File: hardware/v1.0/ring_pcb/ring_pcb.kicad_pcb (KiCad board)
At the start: 2 copper layers, 17.8 x 17.8 mm, 14 parts

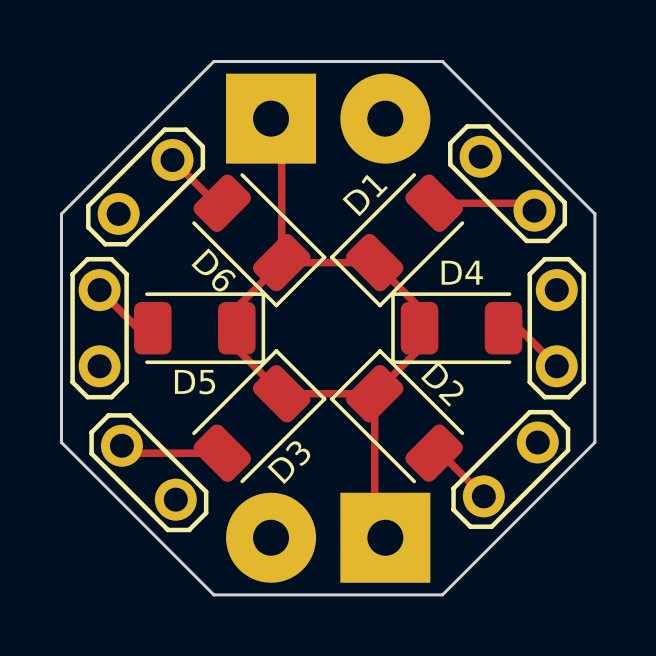
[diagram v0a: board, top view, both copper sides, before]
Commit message: Update pcb to v0.2 for new mounting plan
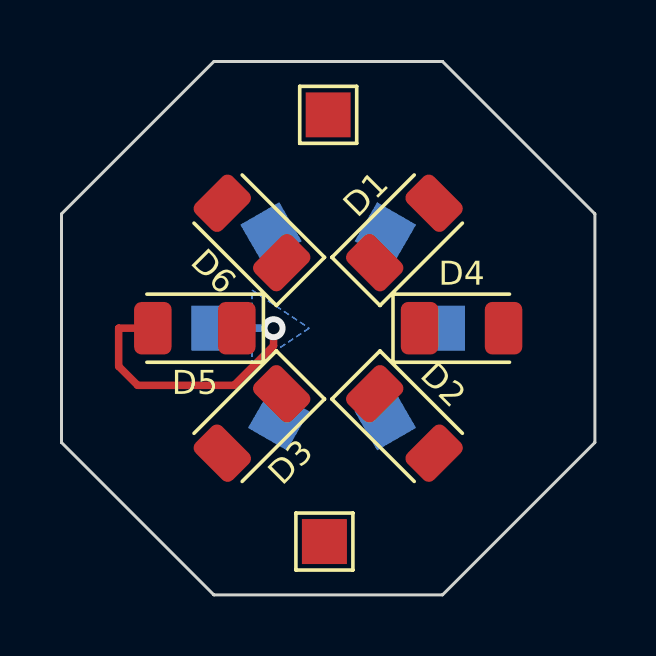
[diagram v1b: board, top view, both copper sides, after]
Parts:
- TP1, TP2, TP3, TP4, TP5, TP6: value TestPoint_2Pole -> TestPoint; footprint TestPoint:TestPoint_2Pads_Pitch2.54mm_Drill0.8mm -> TestPoint:TestPoint_Pad_1.5x1.5mm; moved to B.Cu
- TP7, TP8: value TestPoint_2Pole -> TestPoint; footprint Connector_Wire:SolderWirePad_1x02_P3.81mm_Drill1.2mm -> TestPoint:TestPoint_Pad_1.5x1.5mm
- moved TP2 11.4 mm to (133.3, 99.1), turned to 180 degrees
- moved TP3 11.3 mm to (139.1, 95.9), turned to 60 degrees
- moved TP4 10.2 mm to (135.5, 102.1), turned to 60 degrees
- moved TP5 9.69 mm to (139.1, 102.1), turned to -60 degrees
- moved TP1 5.85 mm to (141.0, 99.1), turned to 180 degrees
- moved TP6 5.12 mm to (135.3, 95.9), turned to -60 degrees
- moved TP8 2.04 mm to (137.0, 106.2), turned to 0 degrees
- moved TP7 1.91 mm to (137.2, 91.9)
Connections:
- D1 pad 1: GND -> Net-(D4-Pad1)
- D2 pad 1: GND -> Net-(D4-Pad1)
- D2 pad 2: Net-(D2-Pad2) -> /N2
- D3 pad 1: GND -> Net-(D4-Pad1)
- D4 pad 1: GND -> Net-(D4-Pad1)
- D5 pad 1: GND -> Net-(D4-Pad1)
- TP1 pad 1: no_connect_8 -> Net-(D4-Pad2)
- TP2 pad 1: no_connect_9 -> Net-(D5-Pad2)
- TP3 pad 1: no_connect_10 -> Net-(D1-Pad2)
- TP4 pad 1: no_connect_11 -> Net-(D3-Pad2)
- TP5 pad 1: no_connect_12 -> /N2
- TP6 pad 1: no_connect_13 -> Net-(D6-Pad2)
- TP7 pad 1: GND -> Net-(D4-Pad1)
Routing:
- net GND: track 27.3 -> 0.00 mm
- net Net-(D5-Pad2): track 2.30 -> 11.0 mm, vias 0 -> 1
- net Net-(D3-Pad2): track 3.45 -> 0.00 mm
- net Net-(D1-Pad2): track 3.45 -> 0.00 mm
- net Net-(D4-Pad2): track 2.30 -> 0.00 mm
- net Net-(D6-Pad2): track 2.26 -> 0.00 mm
- net Net-(D2-Pad2): track 2.26 -> 0.00 mm
- added copper zone on B.Cu, net /N2
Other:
- board text added: "Lantern Ring v0.2 OSHW TAPR designed by whatnick"
- board text removed: "Lantern Ring v0.1 OSHW TAPR designed by whatnick"

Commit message: More vias and keepouts
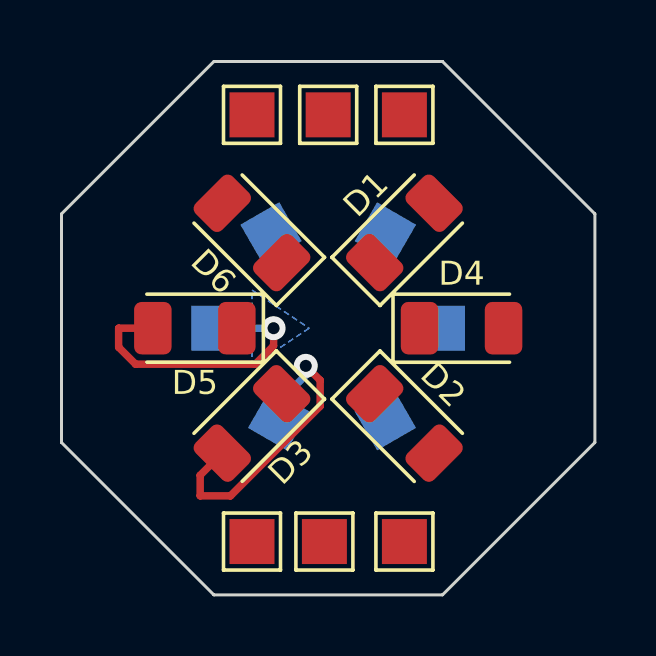
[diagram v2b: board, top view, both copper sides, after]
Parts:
- added TP10: TestPoint, TestPoint:TestPoint_Pad_1.5x1.5mm, F.Cu at (139.7, 91.9)
- added TP11: TestPoint, TestPoint:TestPoint_Pad_1.5x1.5mm, F.Cu at (134.6, 106.2)
- added TP12: TestPoint, TestPoint:TestPoint_Pad_1.5x1.5mm, F.Cu at (134.6, 91.9)
- added TP9: TestPoint, TestPoint:TestPoint_Pad_1.5x1.5mm, F.Cu at (139.7, 106.2)
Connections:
- D1 pad 1: Net-(D4-Pad1) -> GND
- D2 pad 1: Net-(D4-Pad1) -> GND
- D3 pad 1: Net-(D4-Pad1) -> GND
- D4 pad 1: Net-(D4-Pad1) -> GND
- D5 pad 1: Net-(D4-Pad1) -> GND
- TP7 pad 1: Net-(D4-Pad1) -> GND
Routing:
- net Net-(D3-Pad2): track 0.00 -> 10.7 mm, vias 0 -> 1
- net Net-(D5-Pad2): track 11.0 -> 10.0 mm

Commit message: New PCB and Gerbers
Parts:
- moved TP8 0.13 mm to (137.2, 106.2)
- moved TP10 0.05 mm to (139.8, 91.9)
- moved TP11 0.05 mm to (134.6, 106.2)
- moved TP12 0.05 mm to (134.6, 91.9)
- moved TP9 0.05 mm to (139.8, 106.2)
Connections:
- net Net-(D1-Pad2) renamed /N1
- net Net-(D3-Pad2) renamed /N3
- net Net-(D4-Pad2) renamed /N4
- net Net-(D5-Pad2) renamed /N5
- net Net-(D6-Pad2) renamed /N6
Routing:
- net /N1: track 0.00 -> 8.62 mm, vias 0 -> 1
- net /N6: track 0.00 -> 8.32 mm, vias 0 -> 1
- net /N2: track 0.00 -> 7.99 mm, vias 0 -> 1
- net /N4: track 0.00 -> 7.35 mm, vias 0 -> 1
